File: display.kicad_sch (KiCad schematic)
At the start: 0 parts

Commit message: First draft of USB and power module Plus some display started
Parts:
- added J?: 5051102491, 5051102491, symbol E-paper-library:5051102491
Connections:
- new net BS: J?.8
- new net EPD BUSY(CSB): J?.9
- new net EPD CS: J?.12
- new net EPD DC: J?.11
- new net EPD DIN: J?.14
- new net EPD RST: J?.10
- new net EPD SCK: J?.13
- new net GDR: J?.2
- new net RESE: J?.3
- no-connect marks 0 -> 3
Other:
- note added: "7.5 Inch e-paper datasheet"

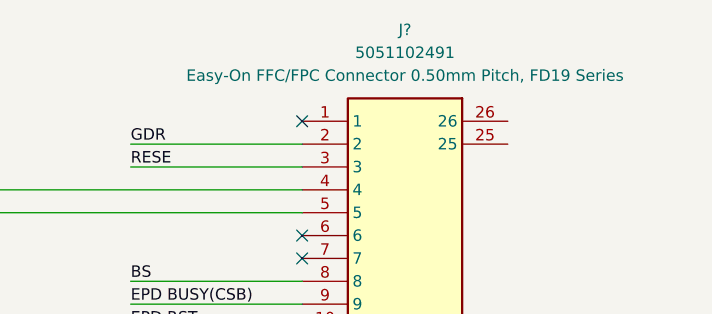
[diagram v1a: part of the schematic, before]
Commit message: Only missing Eframe - Mostly finished MCU - Added Test points to IO - Added LiPo charger - Added Power Source Selection - Added SD card module + SPI connections
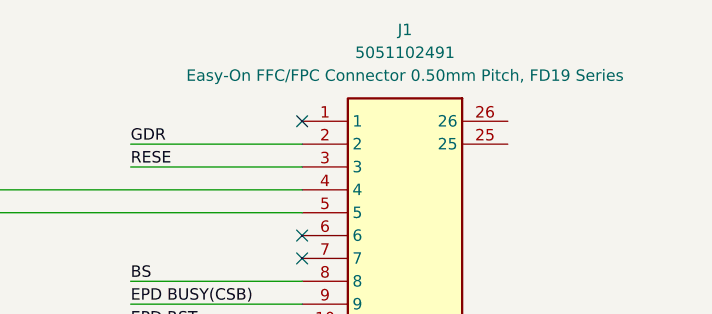
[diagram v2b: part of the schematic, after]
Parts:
- gave numbers to parts that had none: 1
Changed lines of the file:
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@@
 		(dnp no)
 		(fields_autoplaced yes)
-		(property "Reference" "J?"
+		(property "Reference" "J1"
 			(at 180.34 24.13 0)
 			(effects
@@
 			(project "E-paper-picture-frame-HW"
 				(path "/84f37c25-92ec-4cd3-b0ad-d93e10e73cdb/9b514820-994d-4acc-ba3e-efc41ebe2f4e"
-					(reference "J?")
+					(reference "J1")
 					(unit 1)
 				)

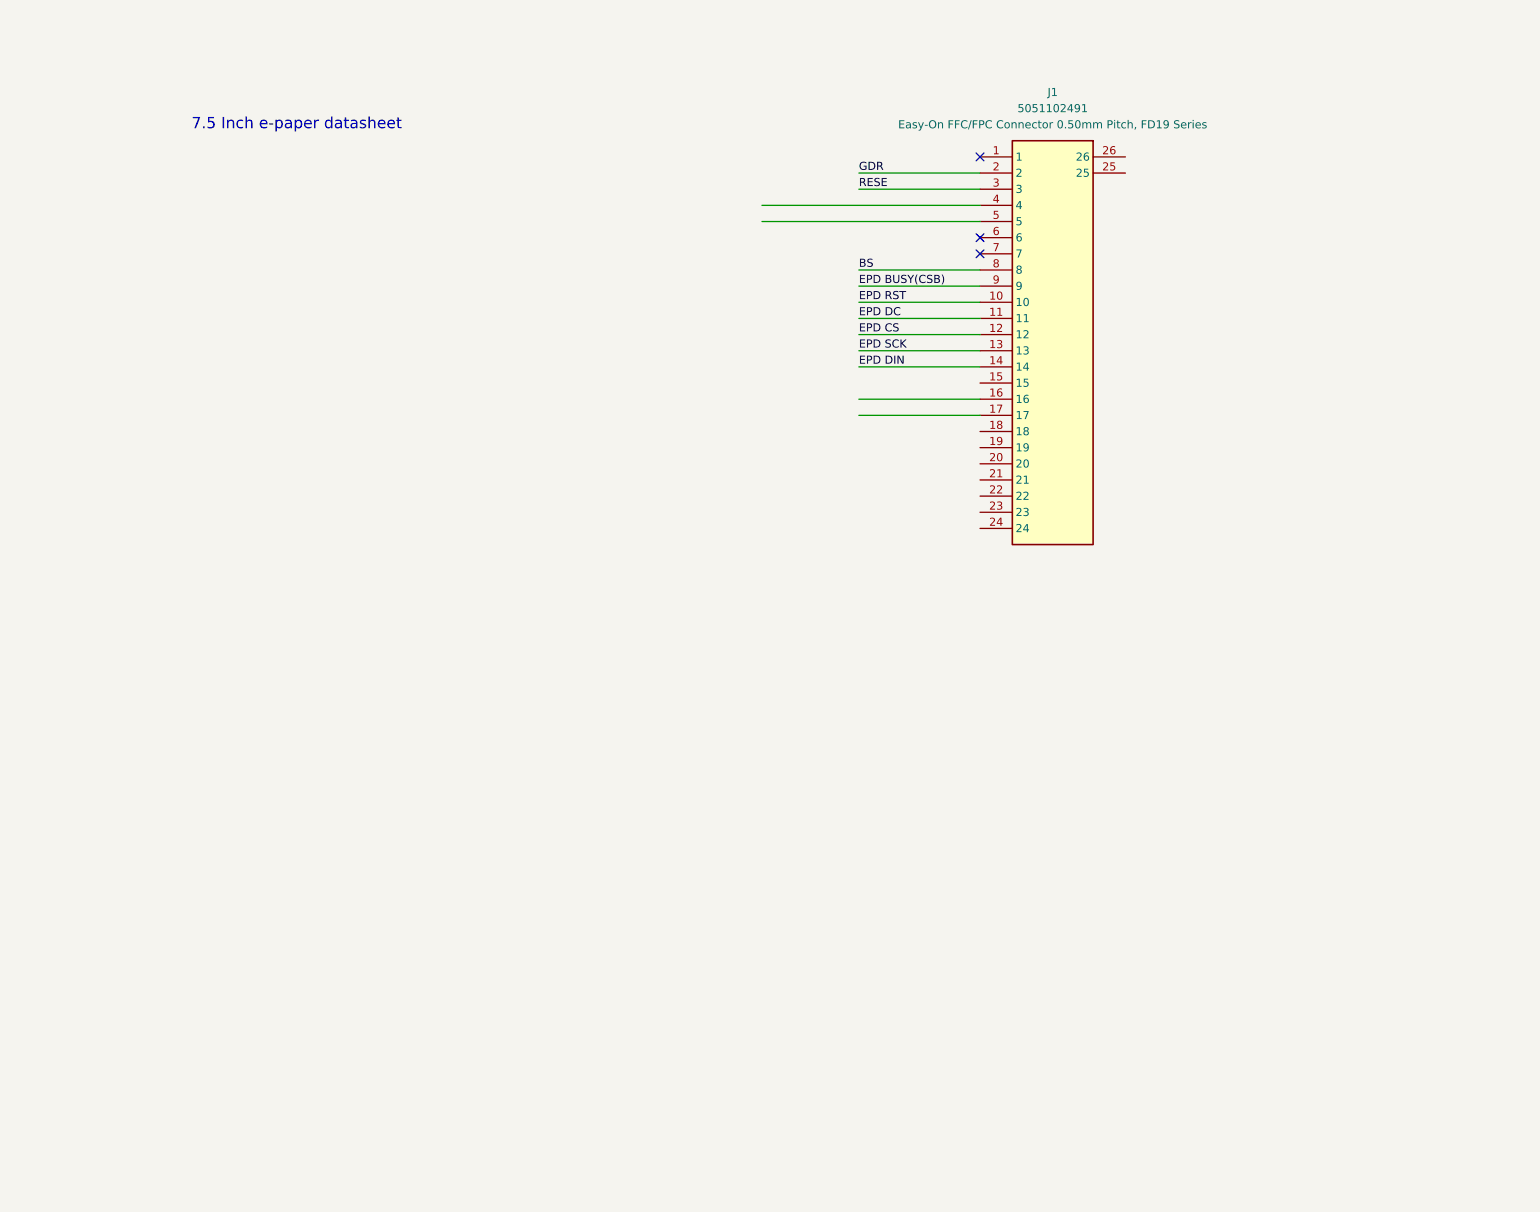
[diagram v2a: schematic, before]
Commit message: Added eframe circuit: - Must replace 10uF caps with higher voltage rated ones - Should double check all the wiring - Assign MCU GPIOs now that all peripherals have their pins assigned
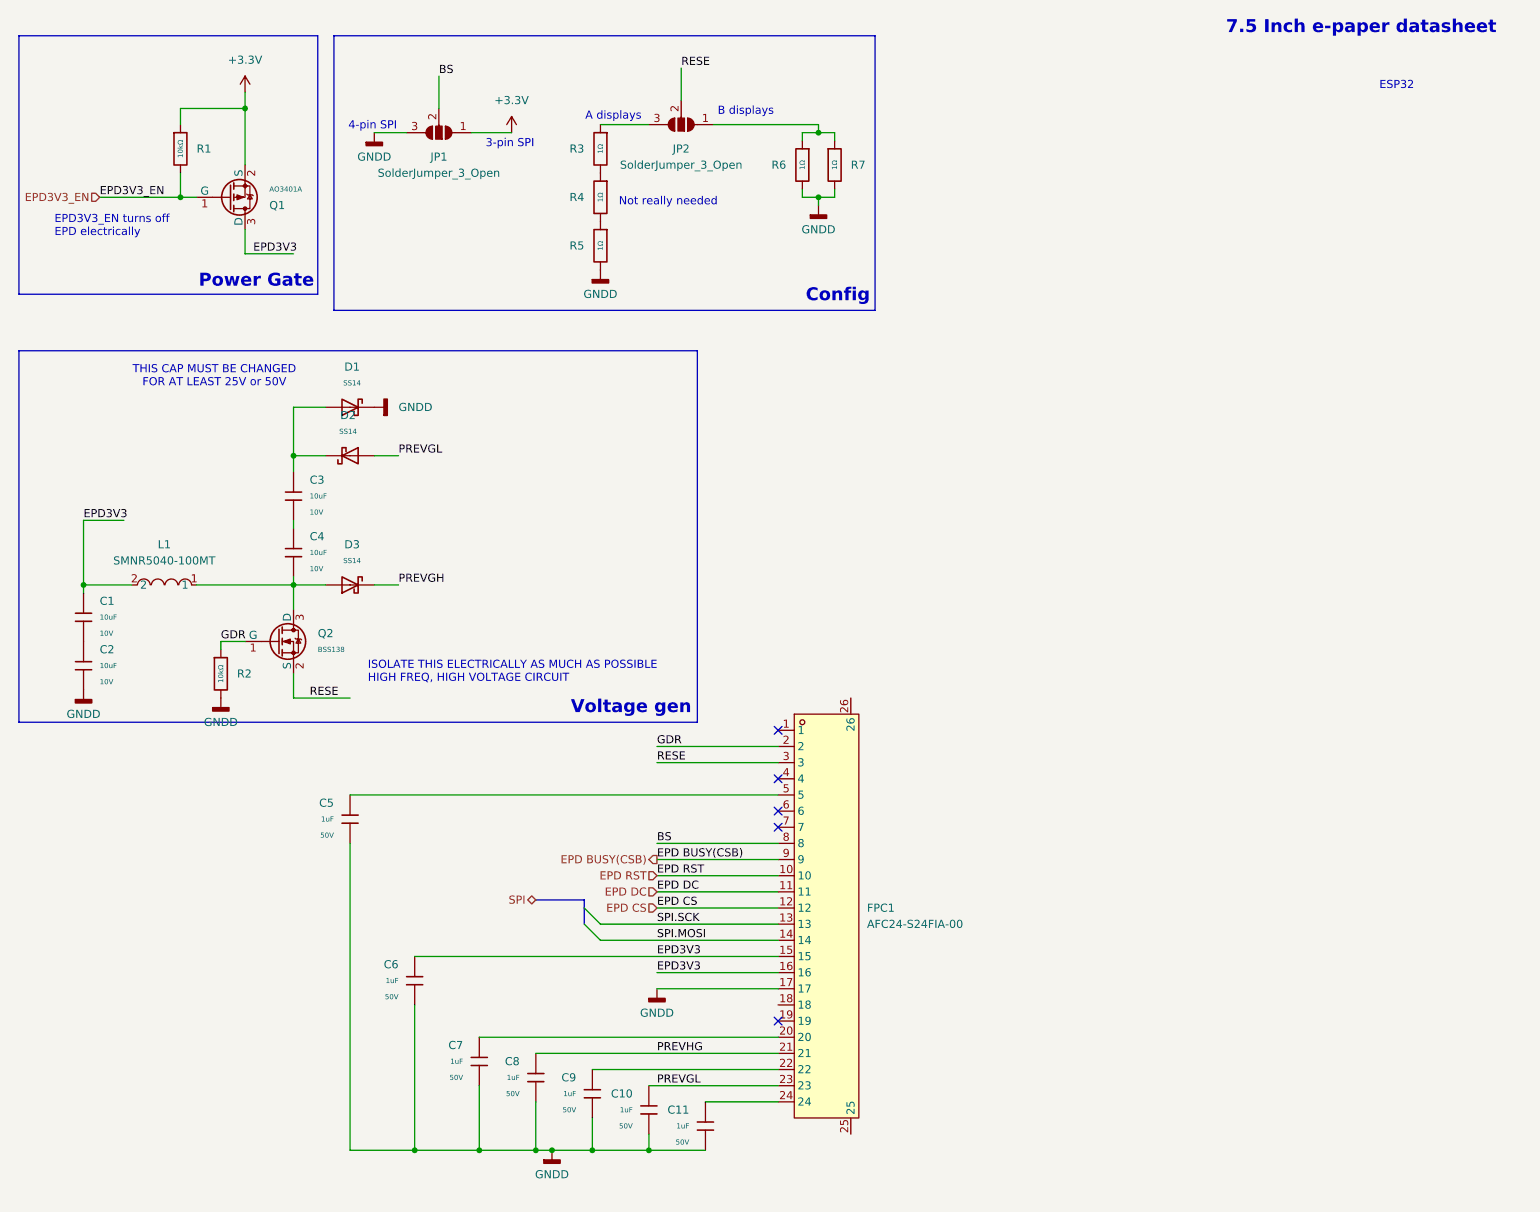
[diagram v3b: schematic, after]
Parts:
- removed J1: 5051102491, 5051102491, symbol E-paper-library:5051102491
- added C1, C2, C3, C4: 10uF, PCM_JLCPCB:C_0603, symbol PCM_JLCPCB-Capacitors:0603,10uF
- added C10, C11, C5, C6, C7, C8, C9: 1uF, PCM_JLCPCB:C_0603, symbol PCM_JLCPCB-Capacitors:0603,1uF
- added D1, D2, D3: SS14, PCM_JLCPCB:D_SMA, symbol PCM_JLCPCB-Diodes:Schottky,SS14
- added FPC1: AFC24-S24FIA-00, FPC:FPC-SMD_P0.50-24P_QCHF-SM-H2.0, symbol E-paper-library:AFC24-S24FIA-00
- added JP1, JP2: SolderJumper_3_Open, symbol Jumper:SolderJumper_3_Open
- added L1: SMNR5040-100MT, L_10uH:IND-SMD_2P-L5.0-W5.0, symbol E-paper-library:SMNR5040-100MT
- added Q1: AO3401A, PCM_JLCPCB:Q_SOT-23, symbol PCM_JLCPCB-Transistors:PMOS,AO3401A
- added Q2: BSS138, PCM_JLCPCB:Q_SOT-23, symbol PCM_JLCPCB-Transistors:NMOS,BSS138
- added R1, R2: 10kΩ, PCM_JLCPCB:R_0402, symbol PCM_JLCPCB-Resistors:0402,10kΩ
- added R3, R4, R5, R6, R7: 1Ω, PCM_JLCPCB:R_0603, symbol PCM_JLCPCB-Resistors:0603,1Ω
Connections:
- net BS: now also FPC1.8, JP1.2 (C)
- net EPD BUSY(CSB): now also FPC1.9
- net EPD CS: now also FPC1.12
- net EPD DC: now also FPC1.11
- net EPD RST: now also FPC1.10
- net GDR: now also FPC1.2, Q2.1 (G), R2.1
- net RESE: now also FPC1.3, JP2.2 (C), Q2.2 (S)
- new net: C7.1, FPC1.20
- new net: C3.2, D1.2, D2.1
- new net: C5.2, FPC1.5
- new net: C3.1, C4.2
- new net: C1.1, C2.2
- new net: R3.2, R4.1
- new net: R4.2, R5.1
- new net: C9.1, FPC1.22
- new net: C11.1, FPC1.24
- new net: JP2.1 (A), R6.1, R7.1
- new net: C4.1, D3.2, L1.1, Q2.3 (D)
- new net: JP2.3 (B), R3.1
- new net +3.3V: JP1.1 (A), Q1.2 (S), R1.1
- new net EPD3V3: C1.2, C6.1, FPC1.15, FPC1.16, L1.2, Q1.3 (D)
- new net EPD3V3_EN: Q1.1 (G), R1.2
- new net GNDD: C10.2, C11.2, C2.1, C5.1, C6.2, C7.2, C8.2, C9.2, D1.1, FPC1.17, JP1.3 (B), R2.2, R5.2, R6.2, R7.2
- new net PREVGH: D3.1
- new net PREVGL: C10.1, D2.2, FPC1.23
- new net PREVHG: C8.1, FPC1.21
- new net SPI.MOSI: FPC1.14
- new net SPI.SCK: FPC1.13
- no-connect marks 3 -> 5
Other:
- note added: "3-pin SPI"
- note added: "4-pin SPI"
- note added: "A displays"
- note added: "B displays"
- note added: "Config"
- note added: "EPD3V3_EN turns off EPD electrically"
- note added: "ESP32"
- note added: "ISOLATE THIS ELECTRICALLY AS MUCH AS POSSIBLE HIGH FREQ, HIGH VOLTAGE CIRCUIT"
- note added: "Not really needed"
- note added: "Power Gate"
- note added: "THIS CAP MUST BE CHANGED FOR AT LEAST 25V or 50V"
- note added: "Voltage gen"

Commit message: Final touches on schematic: Added test points Added LED Fixed symbol footprints
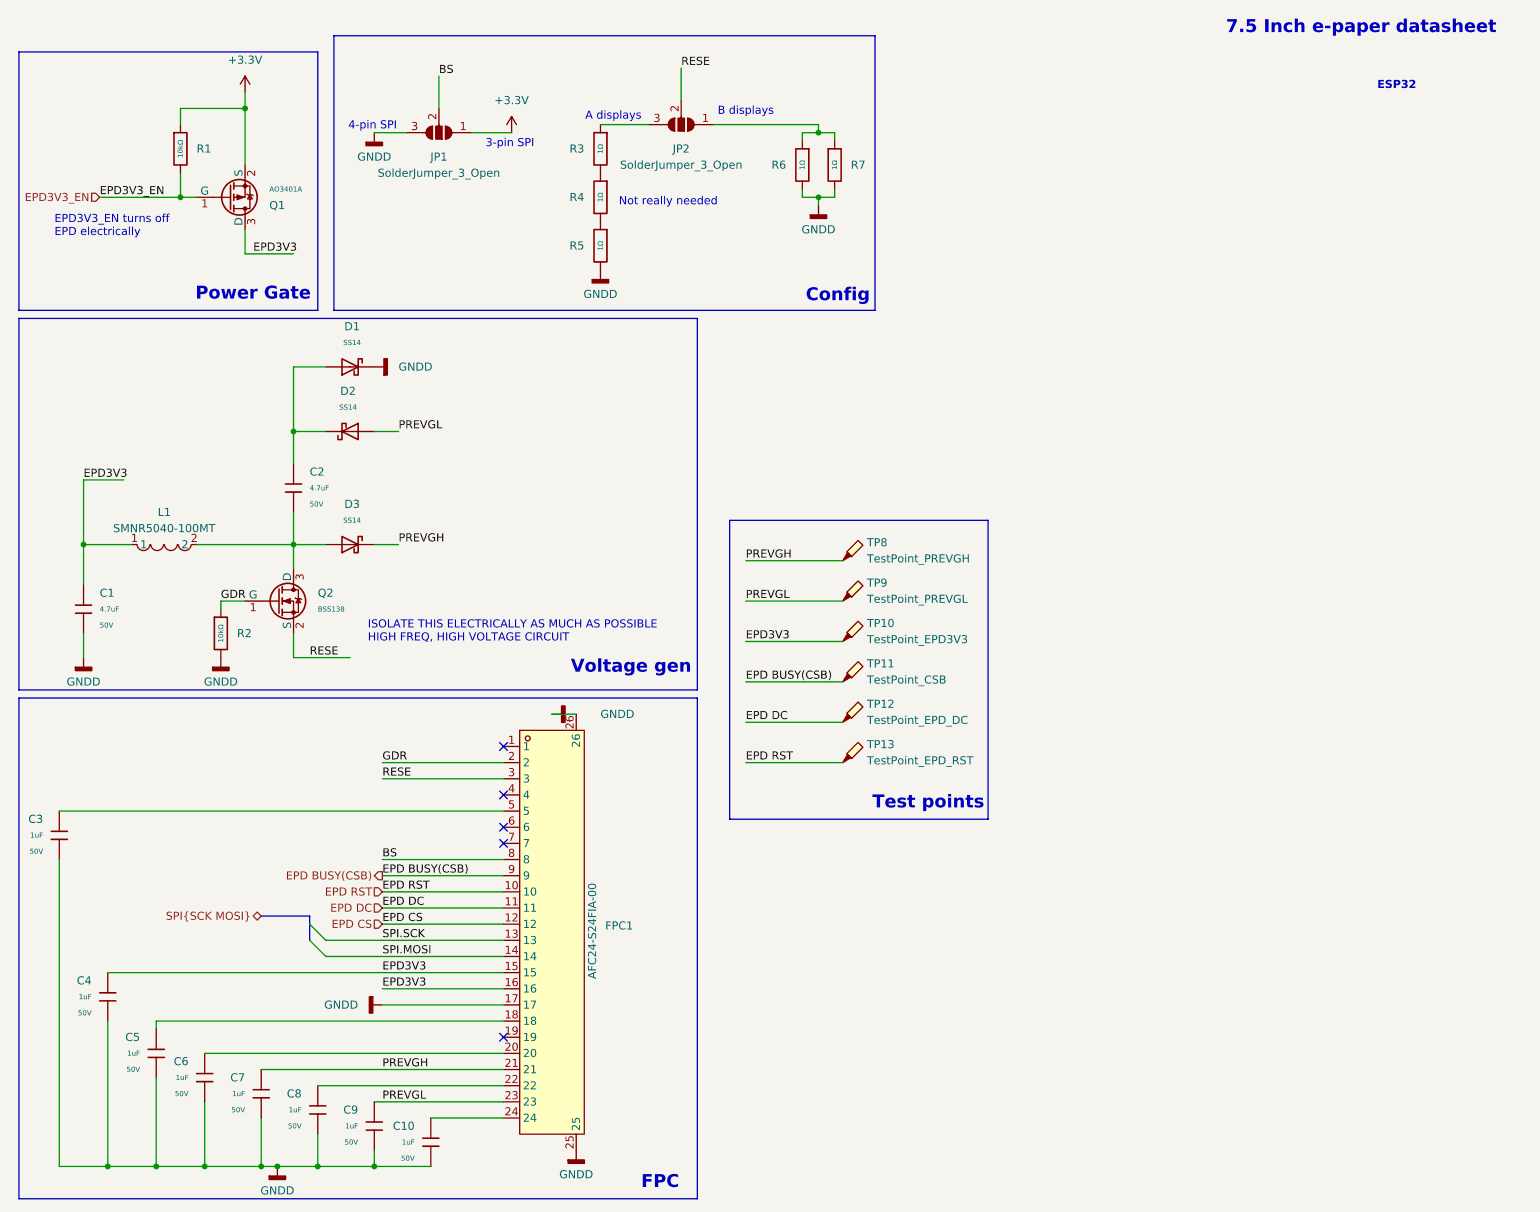
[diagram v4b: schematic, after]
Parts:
- removed C1, C2, C3, C4: 10uF, PCM_JLCPCB:C_0603, symbol PCM_JLCPCB-Capacitors:0603,10uF
- added C1, C2: 4.7uF, PCM_JLCPCB:C_1206, symbol PCM_JLCPCB-Capacitors:1206,4.7uF
- added C5: 1uF, PCM_JLCPCB:C_0603, symbol PCM_JLCPCB-Capacitors:0603,1uF
- added TP10: TestPoint_EPD3V3, TestPoint:TestPoint_Pad_D1.5mm, symbol Connector:TestPoint_Probe
- added TP11: TestPoint_CSB, TestPoint:TestPoint_Pad_D1.5mm, symbol Connector:TestPoint_Probe
- added TP12: TestPoint_EPD_DC, TestPoint:TestPoint_Pad_D1.5mm, symbol Connector:TestPoint_Probe
- added TP13: TestPoint_EPD_RST, TestPoint:TestPoint_Pad_D1.5mm, symbol Connector:TestPoint_Probe
- added TP8: TestPoint_PREVGH, TestPoint:TestPoint_Pad_D1.5mm, symbol Connector:TestPoint_Probe
- added TP9: TestPoint_PREVGL, TestPoint:TestPoint_Pad_D1.5mm, symbol Connector:TestPoint_Probe
- FPC1: footprint FPC:FPC-SMD_P0.50-24P_QCHF-SM-H2.0 -> Libraries:FPC-SMD_P0.50-24P_QCHF-SM-H2.0
- JP1, JP2: footprint (none) -> Jumper:SolderJumper-3_P1.3mm_Open_RoundedPad1.0x1.5mm
- L1: footprint L_10uH:IND-SMD_2P-L5.0-W5.0 -> shielded_ind:IND-SMD_2P-L5.0-W5.0
- renumbered C11 to C10, C5 to C3, C6 to C4, C7 to C6, C8 to C7, C9 to C8, C10 to C9
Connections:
- net PREVHG is gone; now on net PREVGH: C7.1, FPC1.21
- net EPD BUSY(CSB): now also TP11.1
- net EPD DC: now also TP12.1
- net EPD RST: now also TP13.1
- net EPD3V3: now also L1.1, C1.1, TP10.1; no longer L1.2
- net GNDD: now also FPC1.25, FPC1.26, C1.2, C5.2
- net PREVGH: now also TP8.1
- net PREVGL: now also TP9.1
- net at D1.2, D2.1: now also C2.1
- net at FPC1.18: now also C5.1
- net at D3.2, Q2.3 (D): now also L1.2, C2.2; no longer L1.1
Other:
- note added: "FPC"
- note added: "Test points"
- note removed: "THIS CAP MUST BE CHANGED FOR AT LEAST 25V or 50V"
- moved on the sheet: C10, C3, C4, C6, C7, C8, C9, D1, D2, D3, FPC1, Q2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
